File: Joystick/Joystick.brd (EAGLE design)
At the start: 36.3 x 29.8 mm, 13 parts, among them U2 JOYSTICK, U3 ATTINY841

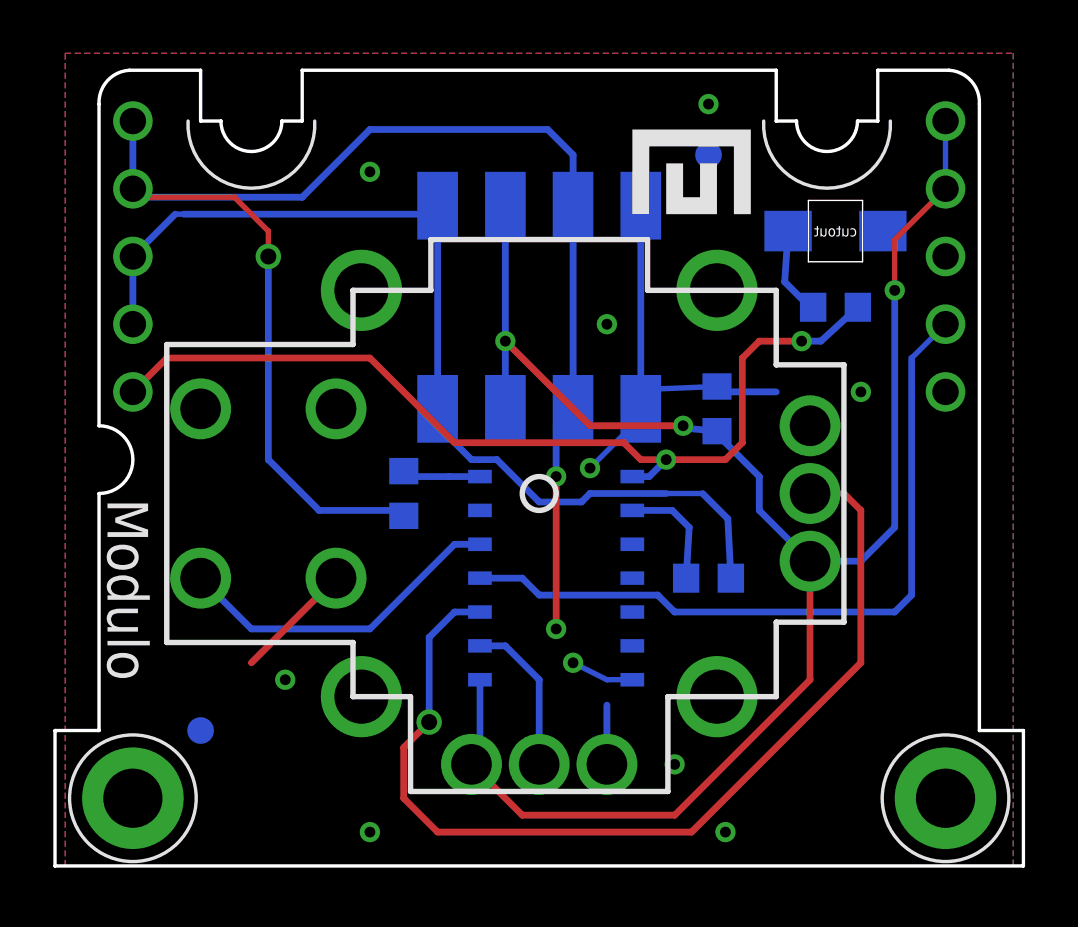
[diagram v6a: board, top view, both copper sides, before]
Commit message: Various small tweaks based on testing and feedback from manufacturer.
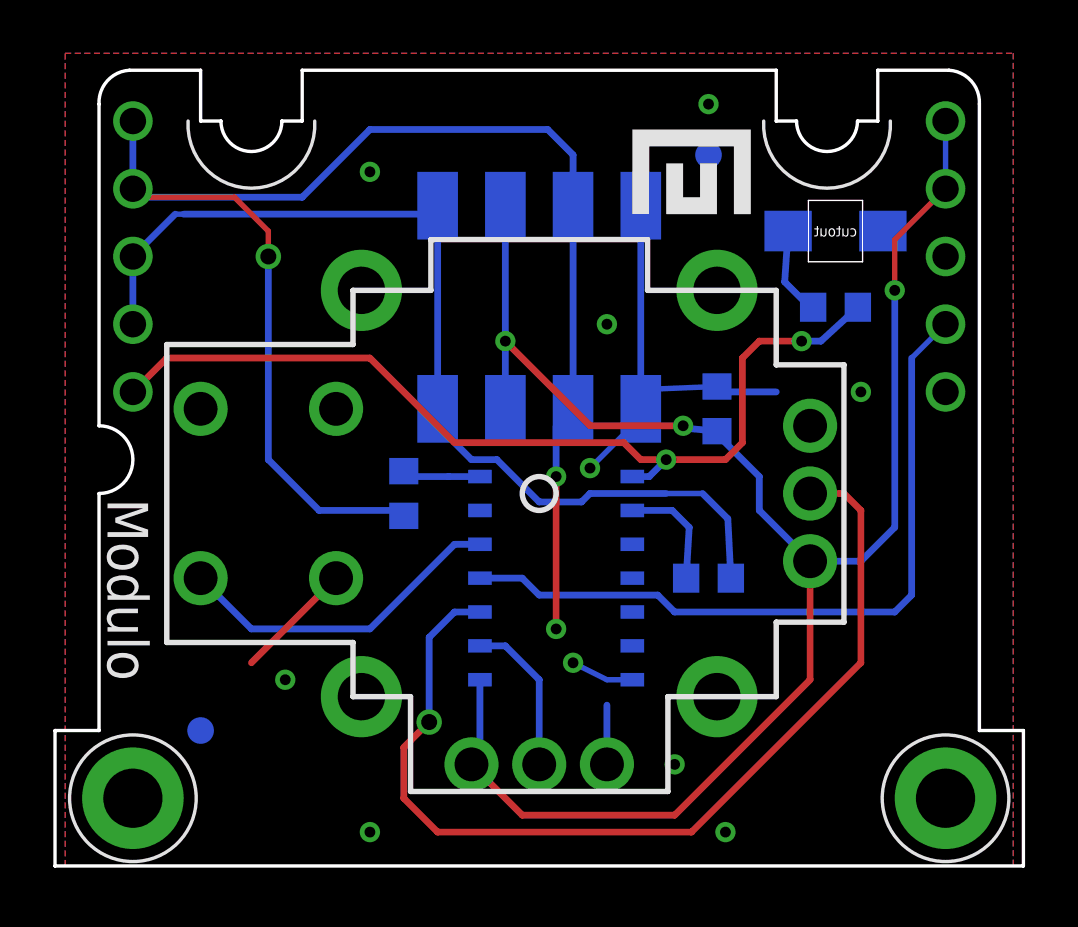
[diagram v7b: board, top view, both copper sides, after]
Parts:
- R8, R9: value 150Ω -> 0Ω
